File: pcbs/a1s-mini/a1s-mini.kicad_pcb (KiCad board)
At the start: 2 copper layers, 58.8 x 55.7 mm, 85 parts, among them J1 UART1, J2 SJ-3524-SMT-TR-PI, J3 Audio Out, J4 UART0, J5 USB4105-GF-A, J6 USB4105-GF-A, Q3 BC818, Q4 MBT3904DW1, Q6 MBT3904DW1, U1 ESP32 A1S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

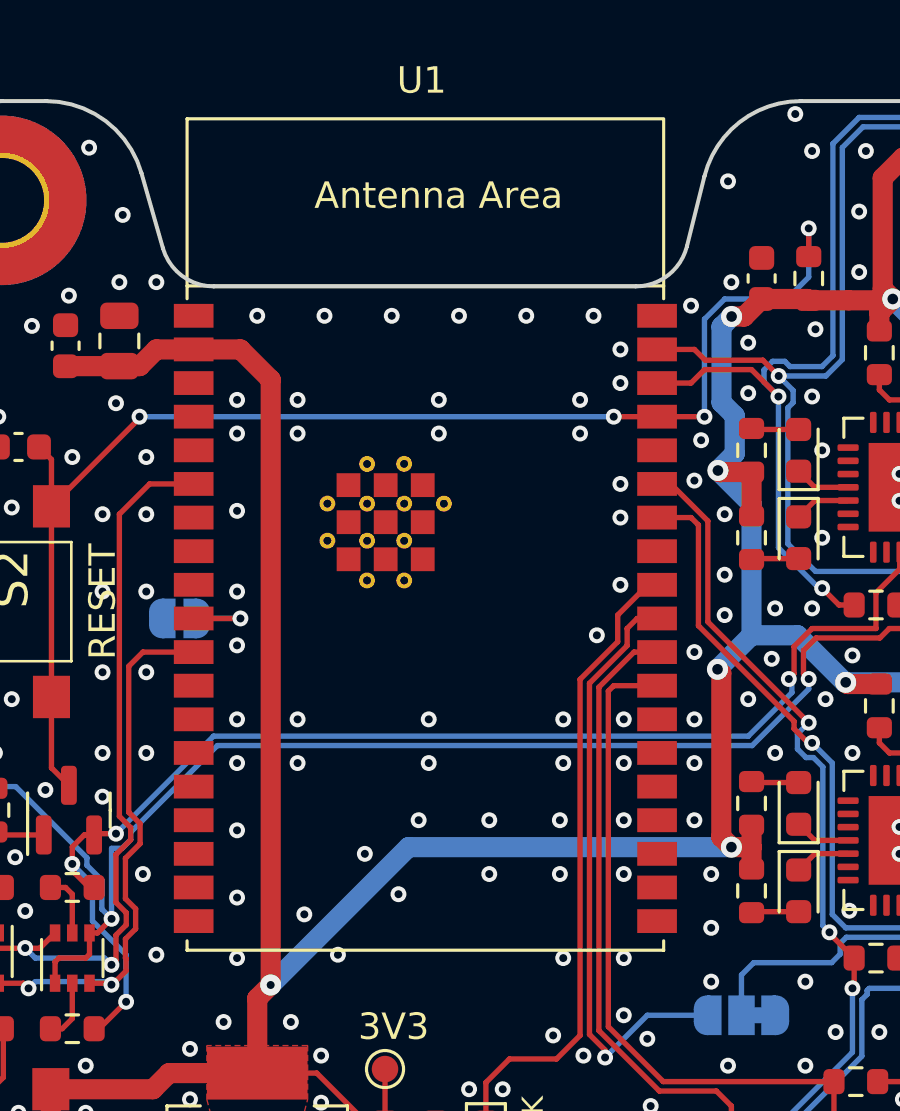
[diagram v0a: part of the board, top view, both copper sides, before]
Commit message: ESP32 A1S outline change
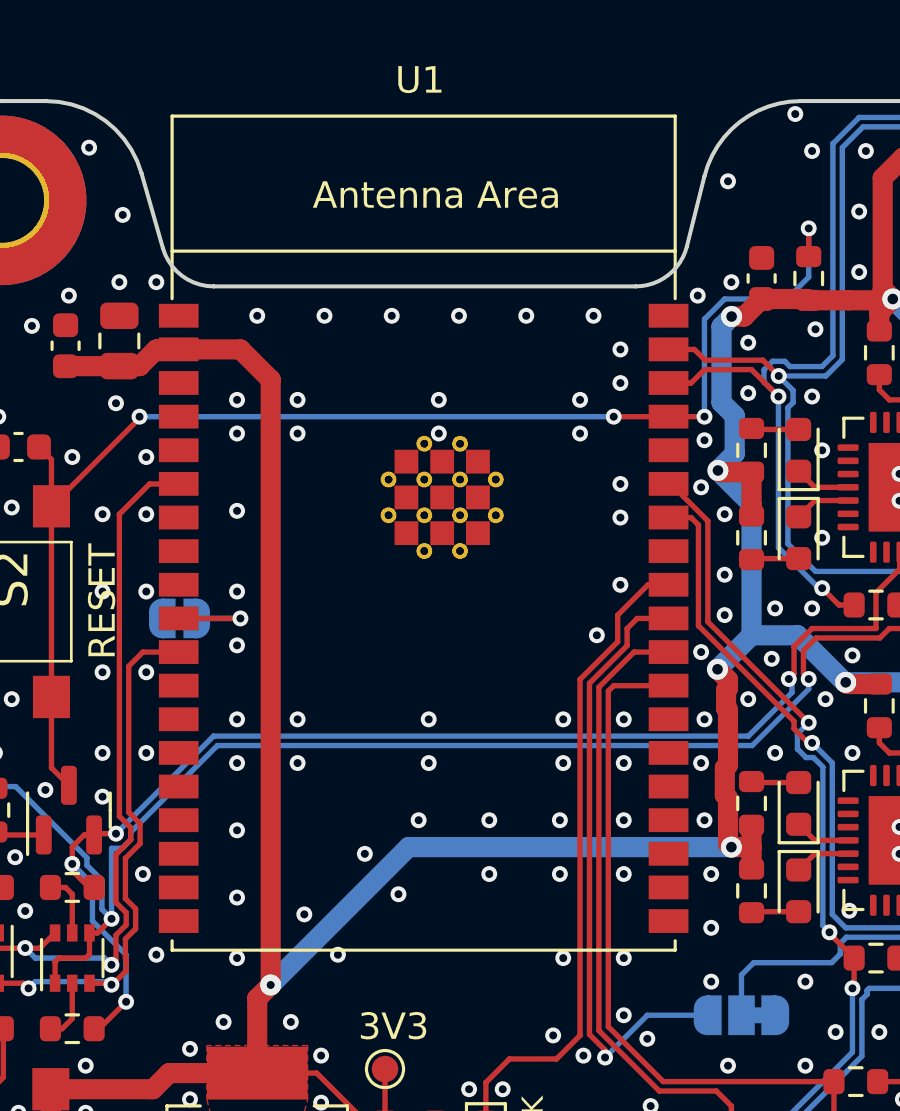
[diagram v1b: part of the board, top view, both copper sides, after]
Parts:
- U1: footprint PCM_Espressif:ESP32-WROVER-E_ThermalVias -> DIY:ESP32-A1S
- moved U1 18.4 mm to (137.2, 112.5)

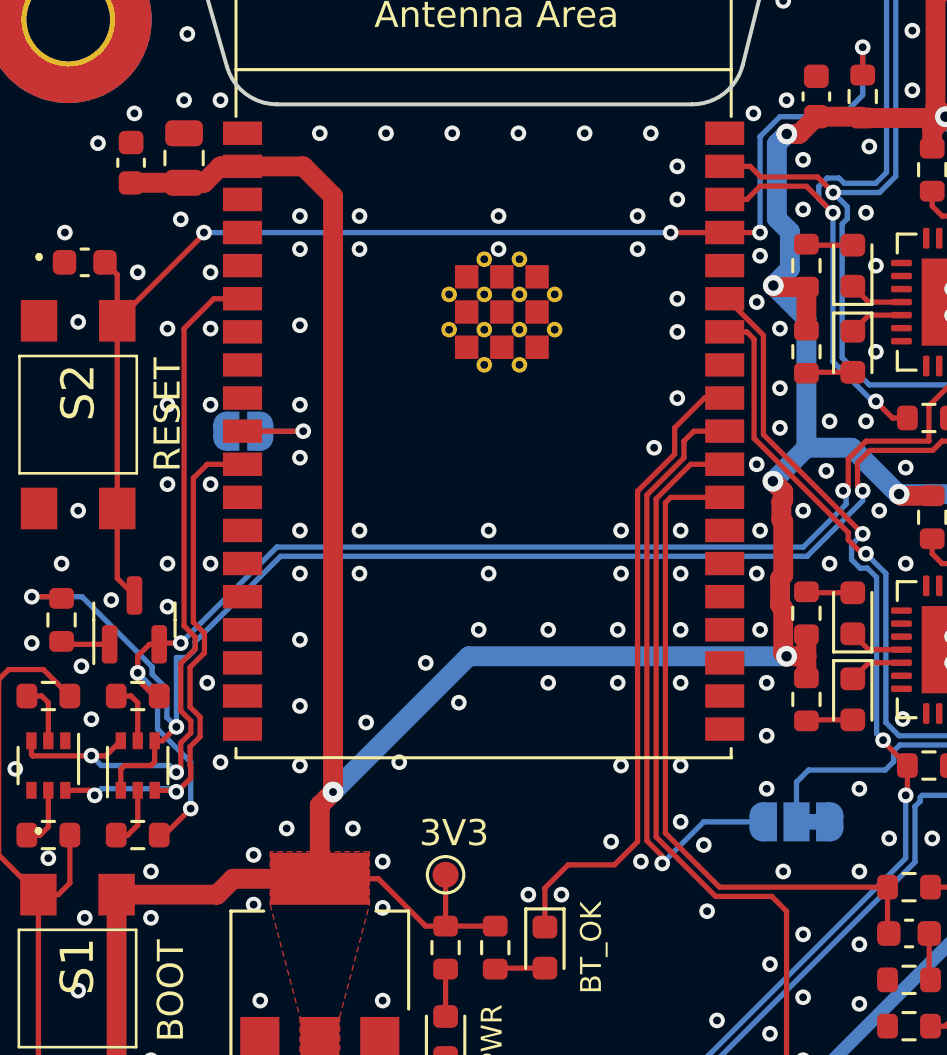
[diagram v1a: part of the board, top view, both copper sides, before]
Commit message: A1S mini corrected, v0.3.0
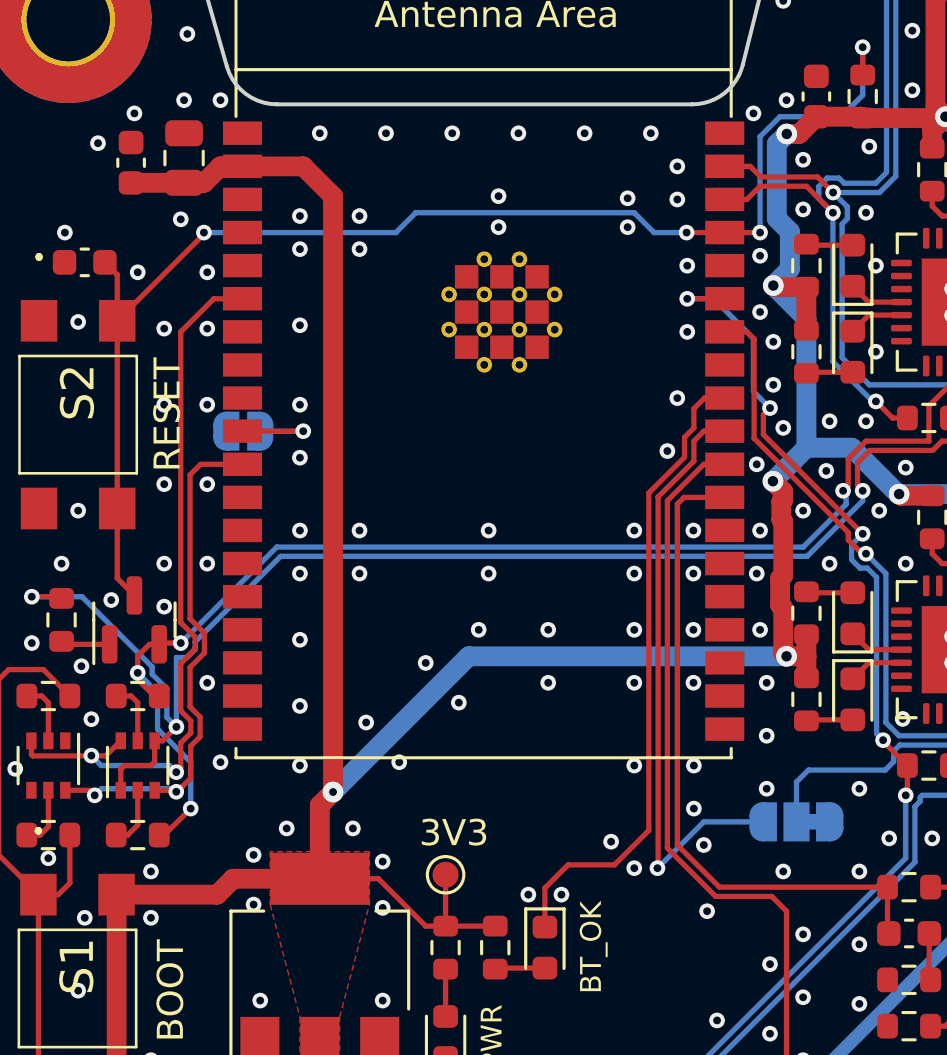
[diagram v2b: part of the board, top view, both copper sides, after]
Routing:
- net TXD1: track 55.8 -> 58.2 mm, vias 4 -> 6
- net IO18: track 24.2 -> 25.1 mm
- net EN: track 50.5 -> 51.2 mm
- net Net-(JP2-A): track 3.42 -> 3.98 mm
